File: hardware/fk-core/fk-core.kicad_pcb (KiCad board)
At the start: 2 copper layers, 26.2 x 105.4 mm, 72 parts, among them J1 S2B-PH-SM4-TB, J2 MICRO-USB, J3 RF-SMA-EDGE, J4 CONN-HDR-1x19, J5 CONN-HDR-1x19, J6 CONN-HDR-2x5, J7 RF-SMA-EDGE, M1 MOUNT_HOLE, M2 MOUNT_HOLE, M3 MOUNT_HOLE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

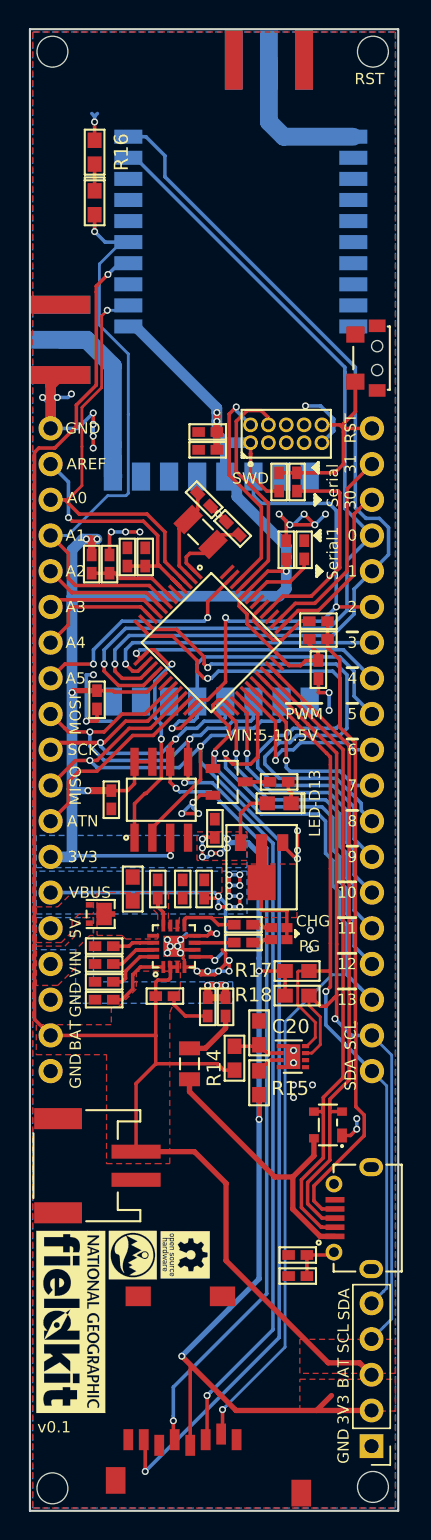
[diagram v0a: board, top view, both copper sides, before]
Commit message: Adding negative logos and one with text.
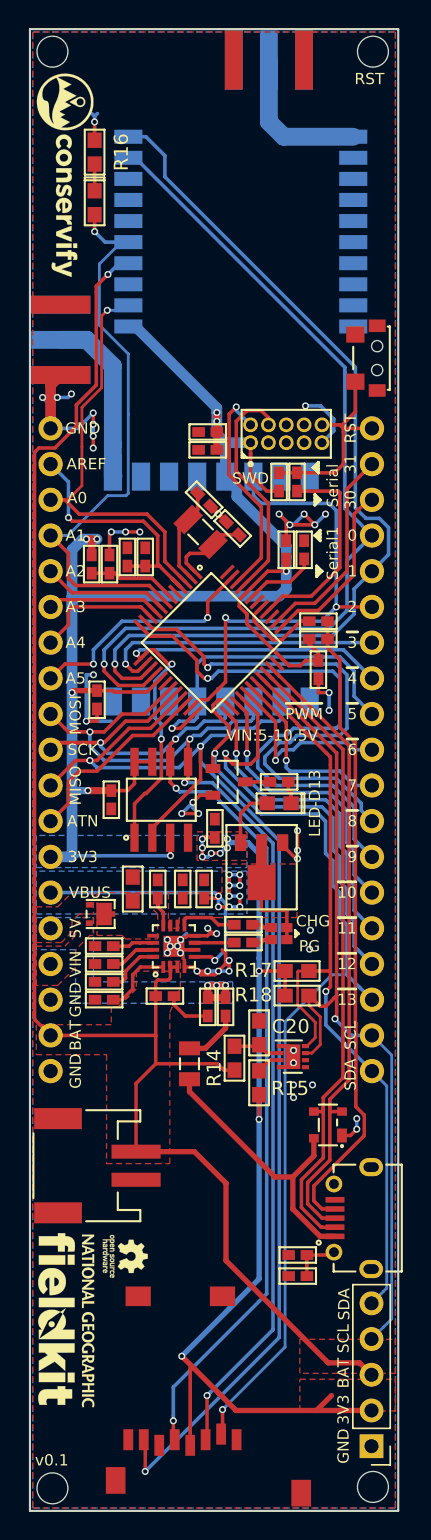
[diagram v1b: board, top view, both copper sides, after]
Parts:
- removed the G*** at (134.1, 135.0)
- removed the G*** at (129.7, 139.8)
- removed the G*** at (137.8, 135.0)
- added G***: LOGO, logos:ngfk_negative_3500, F.Cu at (129.3, 139.7)
- added G***: LOGO, logos:osh_negative_3000, F.Cu at (133.6, 135.1)
- added G***: LOGO, logos:conservify_text_negative_5000, F.Cu at (129.3, 58.2)
